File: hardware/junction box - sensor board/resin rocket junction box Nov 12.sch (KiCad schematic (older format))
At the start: 35 parts, among them J1 Conn_01x08_Female, J10 Conn_01x02_Male, J11 Conn_01x02_Female, J12 Conn_01x03_Male, J13 Conn_01x03_Female, J14 Conn_01x02_Male, J15 Conn_01x02_Female, J16 Conn_01x03_Male, J17 Conn_01x03_Female, J18 Conn_01x06_Female, J19 Conn_01x06_Male, J2 Conn_01x08_Male, J20 Conn_01x06_Female, J21 Conn_01x06_Male, J22 Conn_01x03_Female, J23 Conn_01x03_Male, J24 Conn_01x03_Female, J25 Conn_01x03_Male, J26 Conn_01x04_Male, J3 Conn_01x08_Female, J4 Conn_01x08_Male, J5 2 Male Header Pins (connect t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, J6 Conn_01x04_Male, J7 Conn_01x04_Female, J8 Conn_01x04_Male, J9 Conn_01x04_Female, P1 M3021-000005-2K5PG, P2 M3021-000005-2K5PG, T1 MCP9600, T2 MCP9600, U1 ADS1115IDGS

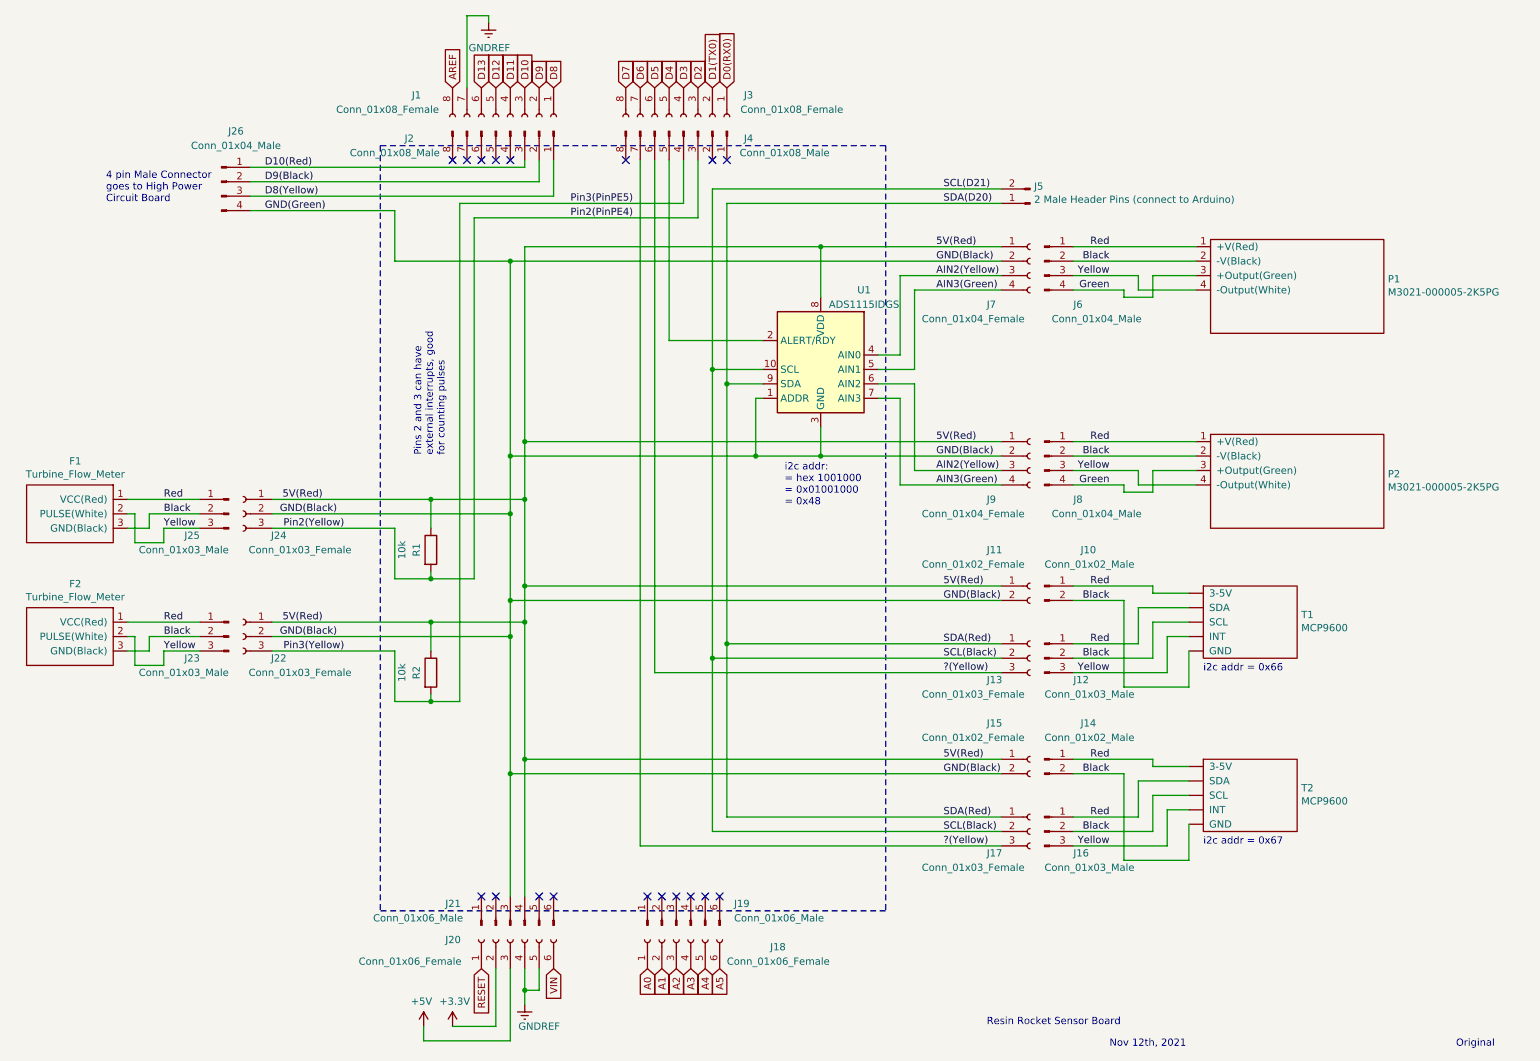
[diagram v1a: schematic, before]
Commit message: Updated Ground Station board, Junction Box sensor board, and Junction Box high power board.
Moved Ground Station pins so that abort (STOP), backup abort (BACKUP_STOP),  auto/manual launch (LAUNCH_MANL_OR_AUTO), and arming (ARM_ROCKET) signals now each go to an Arduino pin that can handle external interrupts. Shifted the rest of the pins so that the manual control pins for SV1, SV2, and IGN1 all connect to the same header on the Arduino. Added battery and outlet for extension cord to key switch circuit. Removed some male header pins because red radio XBee board must connect to them on Arduino instead. As  a consequence, the armed status buzzer/LED pins connect to male headers a level below the board using wires. XBee board also blocks nearest 5V/GND pins, so power must be obtained from the very end of the
Arduino Mega board, using external wires connected to male headers.

Added fuses to high power board. One fuse for each solid state relay, and one fuse from the main 24V high power line.

Corrected wiring for GND, D9, and D8 on sensor board's 4 pin connector (which controls the high power board). Also added a header symbol for the SDA/SCL lines, to indicate that the connections must jump a to a lower board level, down to the Arduino headers, using wires.
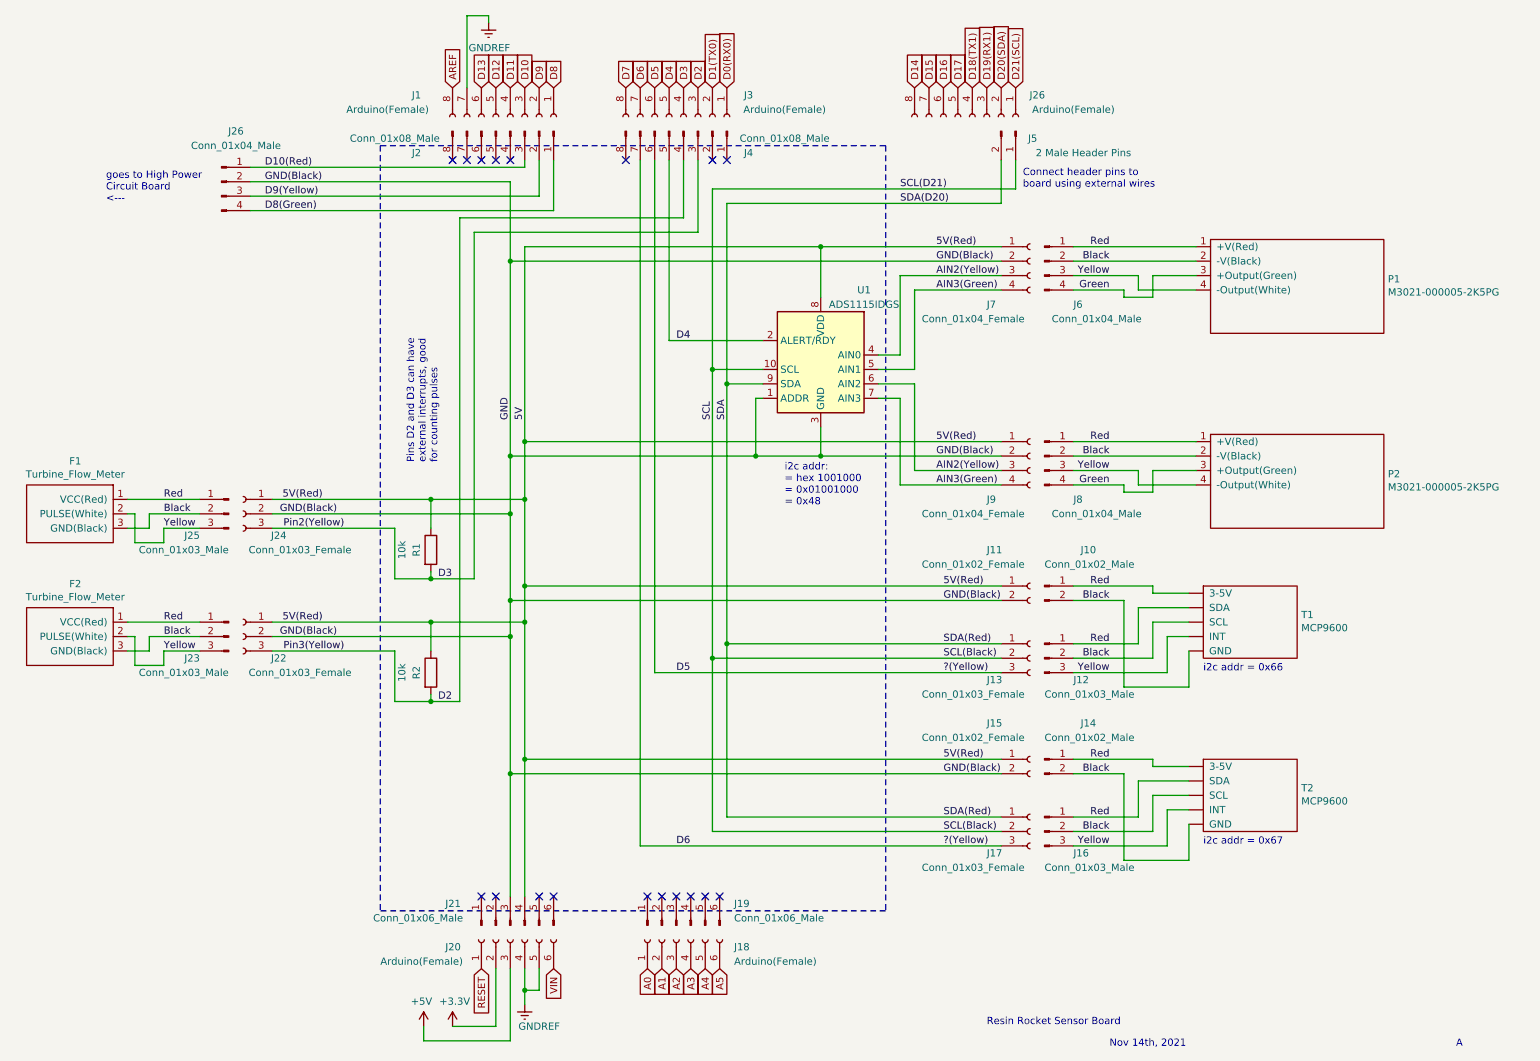
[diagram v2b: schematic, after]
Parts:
- added J26: Arduino(Female), symbol Connector:Conn_01x08_Female
- J1, J3: value Conn_01x08_Female -> Arduino(Female)
- J18, J20: value Conn_01x06_Female -> Arduino(Female)
- J5: value 2 Male Header Pins (connect to Arduino) -> 2 Male Header Pins
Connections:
- net ?(Yellow) is gone; now on net D5: J13.3 (Pin_3), J17.3 (Pin_3), J4.6 (Pin_6), J4.7 (Pin_7)
- net D6 is gone; now on net D5: J3.7 (Pin_7)
- net Pin2(PinPE4) is gone; now on net D3: J24.3 (Pin_3), J4.3 (Pin_3), R1.2
- net Pin3(PinPE5) is gone; now on net D2: J22.3 (Pin_3), J4.4 (Pin_4), R2.2
- net D4: now also J4.5 (Pin_5), U1.2 (ALERT/RDY)
- net 5V(Red) renamed 5V
- net D8(Yellow) renamed D8(Green)
- net D8(Green): now also J26.4 (Pin_4); no longer J26.3 (Pin_3)
- net D9(Black) renamed D9(Yellow)
- net D9(Yellow): now also J26.3 (Pin_3); no longer J26.2 (Pin_2)
- net GND(Black) renamed GND
- net GND: now also J26.2 (Pin_2); no longer J26.4 (Pin_4)
- net SCL(Black) renamed SCL
- net SCL: now also J5.1 (Pin_1); no longer J5.2 (Pin_2)
- net SDA(D20) renamed SDA
- net SDA: now also J5.2 (Pin_2); no longer J5.1 (Pin_1)
- new net D14: J26.8 (Pin_8)
- new net D15: J26.7 (Pin_7)
- new net D16: J26.6 (Pin_6)
- new net D17: J26.5 (Pin_5)
- new net D18(TX1): J26.4 (Pin_4)
- new net D19(RX1): J26.3 (Pin_3)
- new net D20(SDA): J26.2 (Pin_2)
- new net D21(SCL): J26.1 (Pin_1)
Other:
- note added: "A"
- note added: "Connect header pins to \nboard using external wires"
- note added: "Nov 14th, 2021"
- note added: "Pins D2 and D3 can have\nexternal interrupts, good \nfor counting pulses"
- note added: "goes to High Power\nCircuit Board\n<---"
- note removed: "4 pin Male Connector\ngoes to High Power\nCircuit Board"
- note removed: "Nov 12th, 2021"
- note removed: "Original"
- note removed: "Pins 2 and 3 can have\nexternal interrupts, good \nfor counting pulses"
- moved on the sheet: J5
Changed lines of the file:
@@
 U 1 1 61A54FC3
 P 5250 1300
-F 0 "J4" V 5300 1750 50  0000 C CNN
-F 1 "Conn_01x08_Male" V 5400 2000 50  0000 C CNN
+F 0 "J4" V 5400 1750 50  0000 C CNN
+F 1 "Conn_01x08_Male" V 5300 2000 50  0000 C CNN
 F 2 "" H 5250 1300 50  0001 C CNN
 F 3 "~" H 5250 1300 50  0001 C CNN
@@
 U 1 1 61A5C83D
 P 4050 1300
-F 0 "J2" V 4100 600 50  0000 C CNN
-F 1 "Conn_01x08_Male" V 4200 500 50  0000 C CNN
+F 0 "J2" V 4200 650 50  0000 C CNN
+F 1 "Conn_01x08_Male" V 4100 500 50  0000 C CNN
 F 2 "" H 4050 1300 50  0001 C CNN
 F 3 "~" H 4050 1300 50  0001 C CNN
@@
 P 4050 1200
 F 0 "J1" V 3900 550 50  0000 C CNN
-F 1 "Conn_01x08_Female" V 4000 350 50  0000 C CNN
+F 1 "Arduino(Female)" V 4000 350 50  0000 C CNN
 F 2 "" H 4050 1200 50  0001 C CNN
 F 3 "~" H 4050 1200 50  0001 C CNN
@@
 P 5250 1200
 F 0 "J3" V 5100 1650 50  0000 C CNN
-F 1 "Conn_01x08_Female" V 5200 1950 50  0000 C CNN
+F 1 "Arduino(Female)" V 5200 1900 50  0000 C CNN
 F 2 "" H 5250 1200 50  0001 C CNN
 F 3 "~" H 5250 1200 50  0001 C CNN
@@
 U 1 1 61A6DCB8
 P 5200 6900
-F 0 "J18" V 5150 6250 50  0000 R CNN
-F 1 "Conn_01x06_Female" V 5050 6550 50  0000 R CNN
+F 0 "J18" V 5150 6500 50  0000 R CNN
+F 1 "Arduino(Female)" V 5050 6500 50  0000 R CNN
 F 2 "" H 5200 6900 50  0001 C CNN
 F 3 "~" H 5200 6900 50  0001 C CNN
@@
 U 1 1 61A708D4
 P 4050 6900
-F 0 "J20" V 4050 7350 50  0000 R CNN
-F 1 "Conn_01x06_Female" V 3900 7950 50  0000 R CNN
+F 0 "J20" V 4000 7350 50  0000 R CNN
+F 1 "Arduino(Female)" V 3900 7800 50  0000 R CNN
 F 2 "" H 4050 6900 50  0001 C CNN
 F 3 "~" H 4050 6900 50  0001 C CNN
@@
 	1    0    0    -1
 $EndComp
-$Comp
-L Connector:Conn_01x02_Male J5
-U 1 1 61B036AF
-P 7650 1800
-F 0 "J5" H 7622 1682 50  0000 R CNN
-F 1 "2 Male Header Pins (connect to Arduino)" H 7622 1773 50  0000 R CNN
-F 2 "" H 7650 1800 50  0001 C CNN
-F 3 "~" H 7650 1800 50  0001 C CNN
-	1    7650 1800
-	-1   0    0    1
-$EndComp
 Wire Wire Line
 	8300 2400 7950 2400
@@
 	1    0    0    -1
 $EndComp
-Text Label 7050 1700 0    50   ~ 0
-SCL(D21)
-Text Label 7050 1800 0    50   ~ 0
+Text Label 6750 1800 0    50   ~ 0
 SDA(D20)
 Wire Wire Line
@@
 Connection ~ 5450 4950
 Wire Wire Line
-	5250 1800 5250 1500
-Text Label 4900 1800 2    50   ~ 0
-Pin3(PinPE5)
-Wire Wire Line
 	3500 5250 3700 5250
 Connection ~ 3500 5250
 Wire Wire Line
-	5350 1900 5350 1500
-Text Label 4900 1900 2    50   ~ 0
-Pin2(PinPE4)
-Wire Wire Line
 	3800 4400 3500 4400
 Connection ~ 3500 4400
-Text Notes 3600 3550 1    50   ~ 0
-Pins 2 and 3 can have\nexternal interrupts, good \nfor counting pulses
-Wire Wire Line
-	3700 1800 5250 1800
-Wire Wire Line
-	5350 1900 3800 1900
+Text Notes 3550 3600 1    50   ~ 0
+Pins D2 and D3 can have\nexternal interrupts, good \nfor counting pulses
 Wire Wire Line
 	5050 5050 7450 5050
@@
 	5450 1700 5450 2950
 Wire Wire Line
-	5450 1700 7450 1700
-Wire Wire Line
-	7450 1800 5550 1800
-Wire Wire Line
 	5550 1800 5550 3050
-Wire Wire Line
-	3700 1800 3700 5250
-Wire Wire Line
-	3800 4400 3800 1900
 Wire Wire Line
 	5150 2750 5150 1500
@@
 Resin Rocket Sensor Board
 Text Notes 8200 7650 0    50   ~ 0
-Nov 12th, 2021
+Nov 14th, 2021
 Text Notes 10600 7650 0    50   ~ 0
-Original
+A
 NoConn ~ 4050 1500
 Wire Wire Line
@@
 Wire Wire Line
 	4150 1550 2250 1550
-Wire Wire Line
-	4250 1500 4250 1650
-Wire Wire Line
-	4250 1650 2250 1650
-Wire Wire Line
-	2250 1750 4350 1750
-Wire Wire Line
-	4350 1750 4350 1500
 $Comp
 L Connector:Conn_01x04_Male J26
@@
 	1    0    0    -1
 $EndComp
-Wire Wire Line
-	4050 2200 3250 2200
-Wire Wire Line
-	3250 2200 3250 1850
-Wire Wire Line
-	3250 1850 2250 1850
 Connection ~ 4050 2200
 Text Label 2350 1550 0    50   ~ 0
 D10(Red)
 Text Label 2350 1650 0    50   ~ 0
-D9(Black)
+GND(Black)
 Text Label 2350 1750 0    50   ~ 0
-D8(Yellow)
+D9(Yellow)
 Text Label 2350 1850 0    50   ~ 0
-GND(Green)
+D8(Green)
 Text Notes 1250 1800 0    50   ~ 0
-4 pin Male Connector\ngoes to High Power\nCircuit Board
+goes to High Power\nCircuit Board\n<---
+Text GLabel 7550 1000 1    50   Input ~ 0
+D21(SCL)
+Text GLabel 7450 1000 1    50   Input ~ 0
+D20(SDA)
+Text GLabel 7350 1000 1    50   Input ~ 0
+D19(RX1)
+Text GLabel 7250 1000 1    50   Input ~ 0
+D18(TX1)
+Text GLabel 7150 1000 1    50   Input ~ 0
+D17
+Text GLabel 6950 1000 1    50   Input ~ 0
+D15
+Text GLabel 6850 1000 1    50   Input ~ 0
+D14
+$Comp
+L Connector:Conn_01x08_Female J26
+U 1 1 61927238
+P 7250 1200
+F 0 "J26" V 7100 1650 50  0000 C CNN
+F 1 "Arduino(Female)" V 7200 1900 50  0000 C CNN
+F 2 "" H 7250 1200 50  0001 C CNN
+F 3 "~" H 7250 1200 50  0001 C CNN
+	1    7250 1200
+	0    1    1    0
+$EndComp
+Text GLabel 7050 1000 1    50   Input ~ 0
+D16
+Wire Wire Line
+	7550 1500 7550 1700
+Wire Wire Line
+	7450 1500 7450 1800
+Wire Wire Line
+	5450 1700 7550 1700
+Wire Wire Line
+	5550 1800 7450 1800
+Text Label 6750 1700 0    50   ~ 0
+SCL(D21)
+$Comp
+L Connector:Conn_01x02_Male J5
+U 1 1 61B036AF
+P 7550 1300
+F 0 "J5" V 7600 1450 50  0000 R CNN
+F 1 "2 Male Header Pins" V 7700 2100 50  0000 R CNN
+F 2 "" H 7550 1300 50  0001 C CNN
+F 3 "~" H 7550 1300 50  0001 C CNN
+	1    7550 1300
+	0    1    1    0
+$EndComp
+Text Notes 7600 1700 0    50   ~ 0
+Connect header pins to \nboard using external wires
+Wire Wire Line
+	4050 2200 4050 1650
+Wire Wire Line
+	4050 1650 2250 1650
+Wire Wire Line
+	2250 1750 4250 1750
+Wire Wire Line
+	4250 1500 4250 1750
+Wire Wire Line
+	5350 2000 3800 2000
+Wire Wire Line
+	3700 1900 5250 1900
+Text Label 3550 4400 0    50   ~ 0
+D3
+Wire Wire Line
+	3700 1900 3700 5250
+Wire Wire Line
+	4350 1500 4350 1850
+Wire Wire Line
+	2250 1850 4350 1850
+Wire Wire Line
+	5250 1500 5250 1900
+Wire Wire Line
+	5350 1500 5350 2000
+Wire Wire Line
+	3800 2000 3800 4400
+Text Label 3550 5250 0    50   ~ 0
+D2
+Text Label 5450 3300 1    50   ~ 0
+SCL
+Text Label 5550 3300 1    50   ~ 0
+SDA
+Text Label 4050 3300 1    50   ~ 0
+GND
+Text Label 4150 3300 1    50   ~ 0
+5V
+Text Label 5200 5050 0    50   ~ 0
+D5
+Text Label 5200 6250 0    50   ~ 0
+D6
+Text Label 5200 2750 0    50   ~ 0
+D4
 $EndSCHEMATC
